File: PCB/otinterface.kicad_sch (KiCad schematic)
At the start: 43 parts, among them K1 G6K-2F-Y-5V, Q1 BC857C, Q10 BC847C, Q11 BC857C, Q12 BC847C, Q2 BC847C, Q4 BC857C, Q5 BC857C, Q6 BC857C, Q7 BC857C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

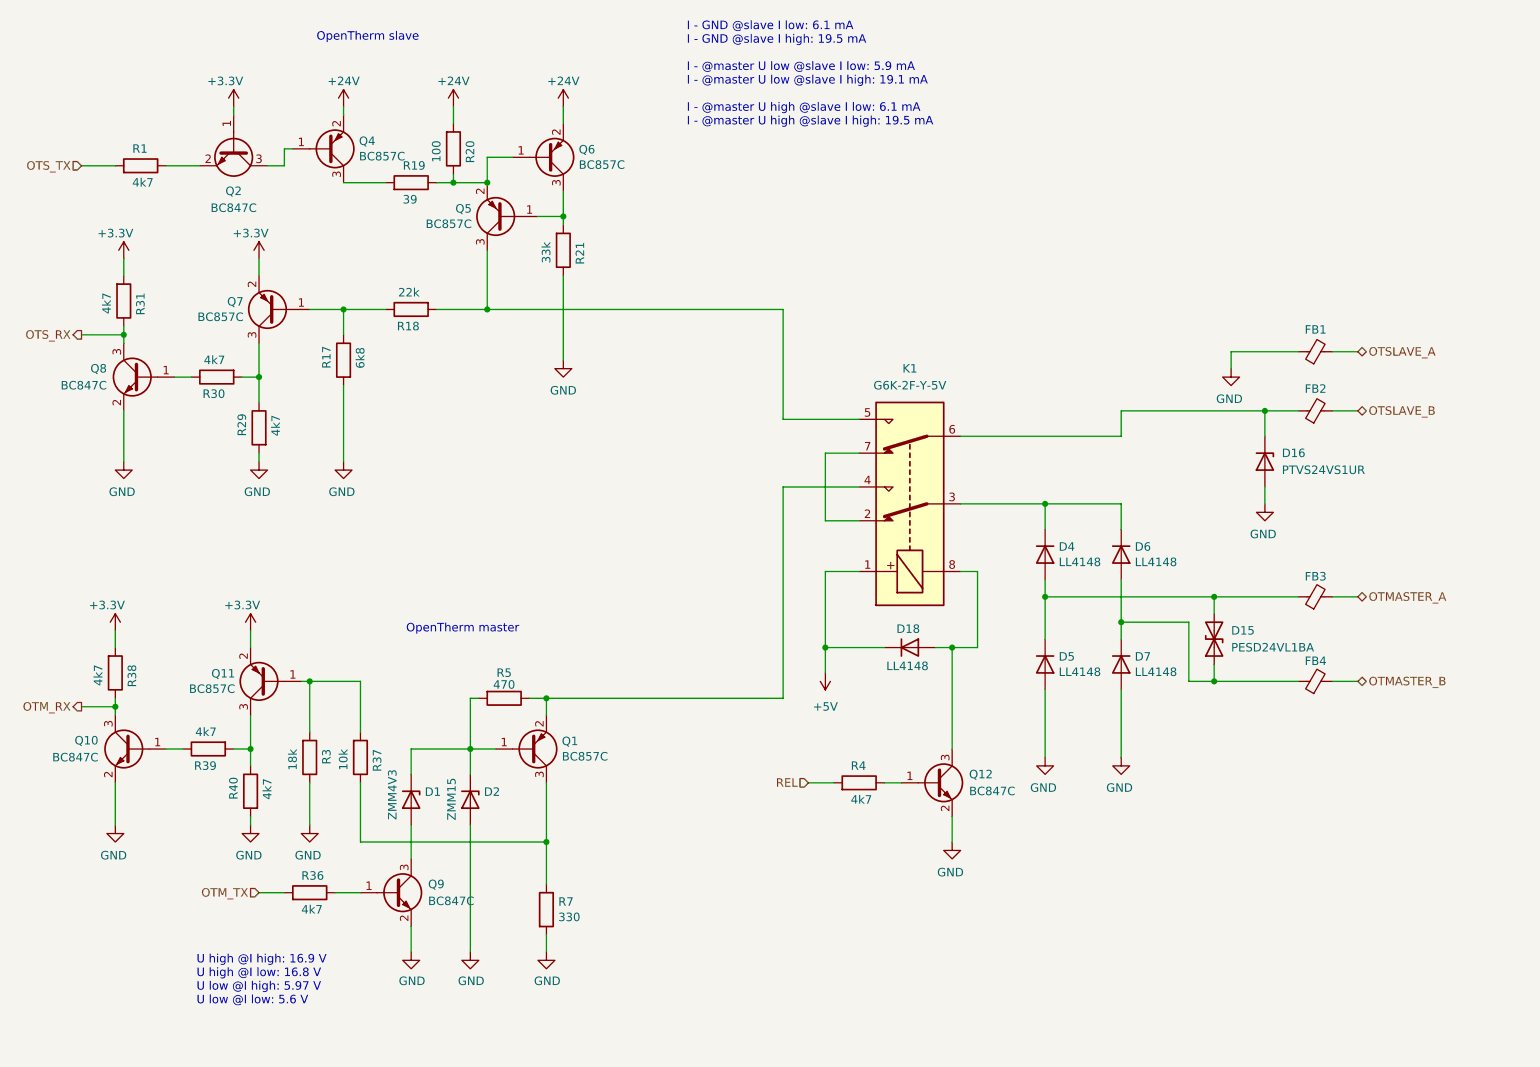
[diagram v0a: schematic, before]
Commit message: sensors for flame / pausetime per cycle aux input sensor
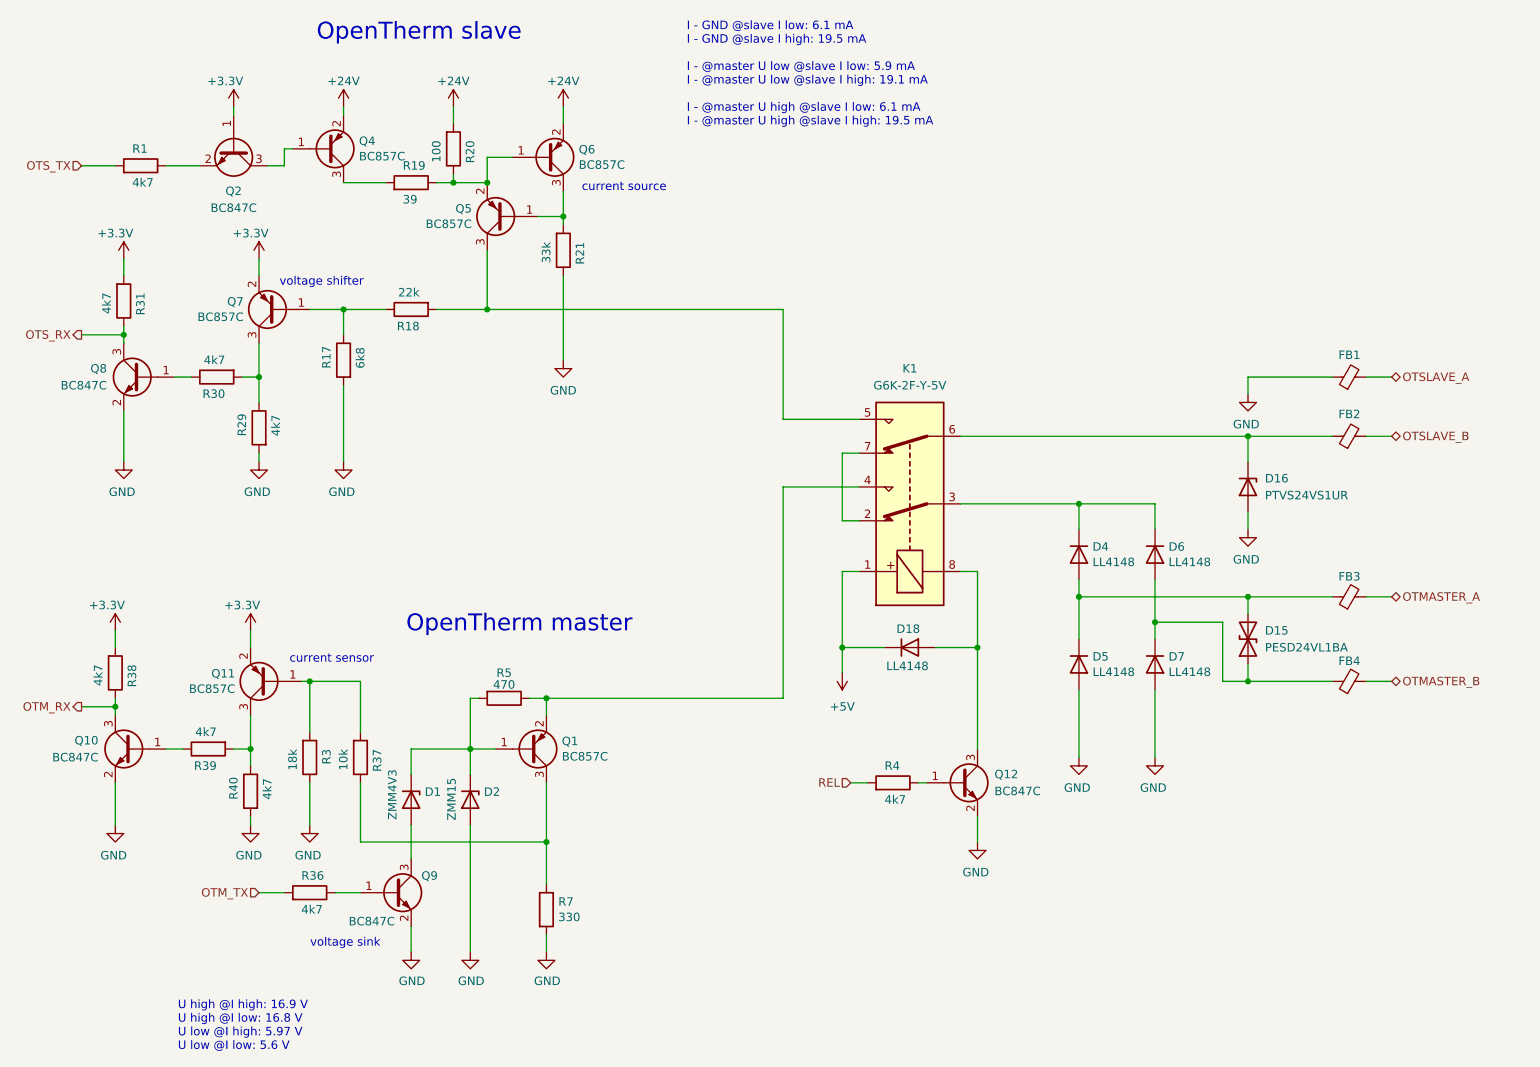
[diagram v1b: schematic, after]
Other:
- note added: "current sensor"
- note added: "current source"
- note added: "voltage shifter"
- note added: "voltage sink"
- title: OT Thing -> OTthing
- moved on the sheet: D15, D16, D4, D5, D6, D7, FB1, FB2, FB3, FB4, Q12, R4

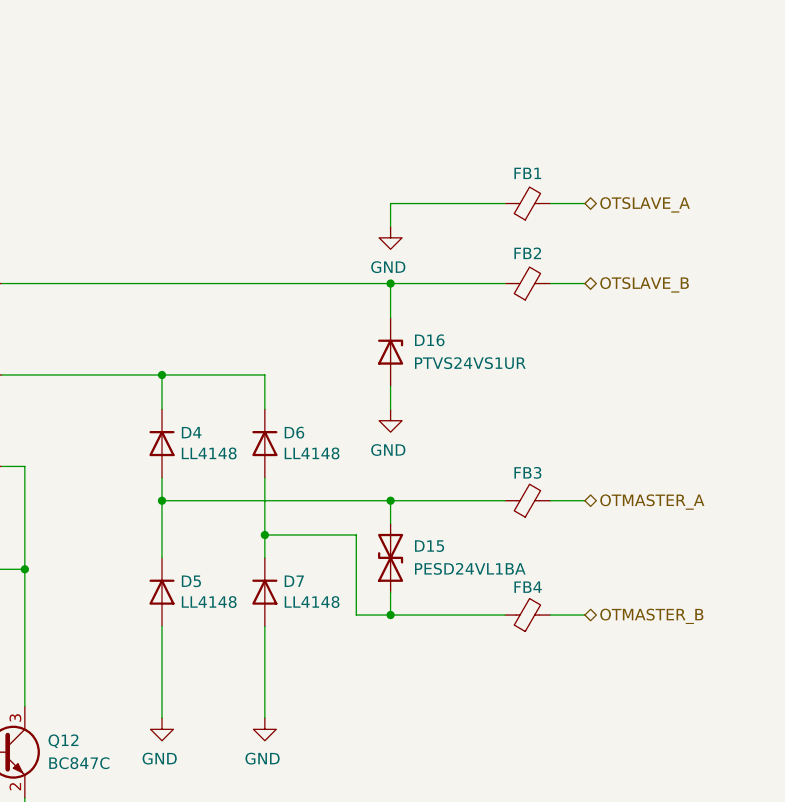
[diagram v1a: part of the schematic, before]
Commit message: add fiducals
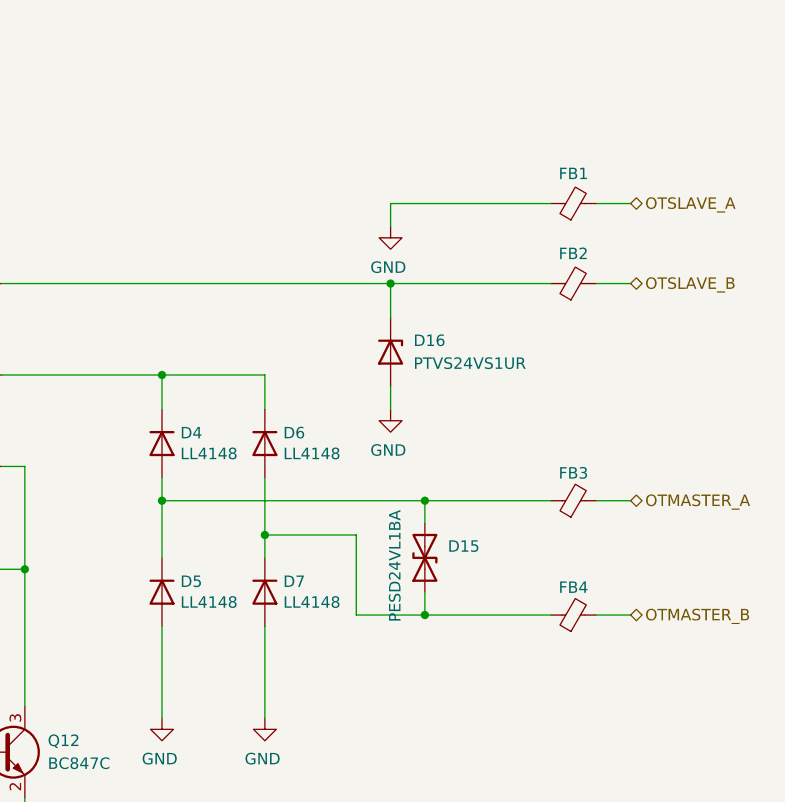
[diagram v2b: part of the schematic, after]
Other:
- moved on the sheet: D15, FB1, FB2, FB3, FB4

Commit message: Migrate to KiCad 10
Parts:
- FB1, FB2, FB3, FB4: value ~ -> (none)
